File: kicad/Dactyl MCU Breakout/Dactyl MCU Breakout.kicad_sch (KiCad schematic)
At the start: 0 parts

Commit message: feat: schema and board: matrix display led split
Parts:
- added D1, D2, D3, D4: SK6812-MINI-E, Dactyl:SK6812-MINI-E-Dog2, symbol Dactyl:SK6812-MINI-E
- added H1, H2: MountingHole, MountingHole:MountingHole_3.2mm_M3_DIN965_Pad, symbol Mechanical:MountingHole
- added H3: MountingHole, Dactyl:ToolingHole_1.152mm, symbol Mechanical:MountingHole
- added J1: Columns, Connector_PinHeader_2.54mm:PinHeader_1x06_P2.54mm_Vertical, symbol Connector_Generic:Conn_01x06
- added J2: Rows, Connector_PinHeader_2.54mm:PinHeader_1x06_P2.54mm_Vertical, symbol Connector_Generic:Conn_01x06
- added J3: Thumbs, Connector_PinHeader_2.54mm:PinHeader_1x06_P2.54mm_Vertical, symbol Connector_Generic:Conn_01x06
- added J4: Display, Connector_PinHeader_2.54mm:PinHeader_1x05_P2.54mm_Vertical, symbol Connector_Generic:Conn_01x05
- added J5: Split, Connector_PinHeader_2.54mm:PinHeader_1x03_P2.54mm_Vertical, symbol Connector_Generic:Conn_01x03
- added J6: Extrernal, Connector_PinHeader_2.54mm:PinHeader_1x04_P2.54mm_Vertical, symbol Connector_Generic:Conn_01x04
- added J7: JST, Dactyl:JST_PH_S2B-PH-K_1x02_P2.00mm_Horizontal, symbol Dactyl:Conn_01x02_Jump_Two_Side
- added J8: Encoder, Connector_PinHeader_2.54mm:PinHeader_1x02_P2.54mm_Vertical, symbol Connector_Generic:Conn_01x02
- added JP1: LED2 cutoff, Jumper:SolderJumper-2_P1.3mm_Bridged_RoundedPad1.0x1.5mm, symbol Jumper:SolderJumper_2_Bridged
- added JP2: LED3 cutoff, Jumper:SolderJumper-2_P1.3mm_Bridged_RoundedPad1.0x1.5mm, symbol Jumper:SolderJumper_2_Bridged
- added JP3: LED4 cutoff, Jumper:SolderJumper-2_P1.3mm_Bridged_RoundedPad1.0x1.5mm, symbol Jumper:SolderJumper_2_Bridged
- added JP4: External Row Select, Jumper:SolderJumper-3_P1.3mm_Bridged12_RoundedPad1.0x1.5mm, symbol Jumper:SolderJumper_3_Bridged12
- added SW1: Reset, Dactyl:SW_Tactile_SKHL_Angled, symbol Switch:SW_Push
- added SW2: Battery, Dactyl:SW_SPDT_JS202011AQN_wider, symbol Switch:SW_SPDT
- added SW3: LED, Dactyl:SW_SPDT_JS202011AQN_wider, symbol Switch:SW_SPDT
- added U1: ProMicro_r, Dactyl:ProMicro_v2, symbol Dactyl:ProMicro_r
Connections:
- new net: D4.1 (VDD), JP3.2 (B)
- new net: D3.2 (DOUT), D4.4 (DIN)
- new net: J6.4 (Pin_4), JP4.2 (C)
- new net: D2.2 (DOUT), D3.4 (DIN)
- new net: D1.2 (DOUT), D2.4 (DIN)
- new net: D3.1 (VDD), JP2.2 (B), JP3.1 (A)
- new net CS: J4.1 (Pin_1), U1.8 (C6/5)
- new net GND: D1.3 (VSS), D2.3 (VSS), D3.3 (VSS), D4.3 (VSS), J4.2 (Pin_2), J5.3 (Pin_3), J7.GND, SW1.2, U1.23 (GND), U1.3 (GND), U1.4 (GND)
- new net LED: D1.4 (DIN), U1.7 (D4/4)
- new net MOSI: J4.5 (Pin_5), U1.6 (SCL/D0/3)
- new net RAW: J5.2 (Pin_2), SW2.1 (A), U1.24 (RAW)
- new net RST: SW1.1, U1.22 (RST)
- new net SCK: J4.4 (Pin_4), U1.5 (SDA/D1/2)
- new net VCC: J4.3 (Pin_3), SW3.2 (B), U1.21 (VCC)
- new net VCC_LED1: D1.1 (VDD), JP1.1 (A), SW3.1 (A)
- new net VCC_LED2: D2.1 (VDD), JP1.2 (B), JP2.1 (A)
- new net bat+: J7.Pos, SW2.2 (B)
- new net col0: J1.1 (Pin_1), J3.1 (Pin_1), J6.1 (Pin_1), U1.20 (A3/F4)
- new net col1: J1.2 (Pin_2), J3.2 (Pin_2), U1.19 (A2/F5)
- new net col2: J1.3 (Pin_3), J3.3 (Pin_3), U1.18 (A1/F6)
- new net col3: J1.4 (Pin_4), J3.4 (Pin_4), U1.17 (A0/F7)
- new net col4: J1.5 (Pin_5), J3.5 (Pin_5), J6.2 (Pin_2), U1.16 (15/B1)
- new net col5: J1.6 (Pin_6), J6.3 (Pin_3), U1.15 (14/B3)
- new net data: J5.1 (Pin_1), U1.2 (D2/RX1)
- new net enc_b: J8.2 (Pin_2), U1.13 (10/B6)
- new net row0: J2.1 (Pin_1), U1.1 (D3/TX0)
- new net row1: J2.2 (Pin_2), U1.9 (D7/6)
- new net row2: J2.3 (Pin_3), U1.10 (E6/7)
- new net row3: J3.6 (Pin_6), U1.11 (B4/8)
- new net row4: J2.5 (Pin_5), JP4.1 (A), U1.12 (B5/9)
- new net row5: J2.6 (Pin_6), J8.1 (Pin_1), JP4.3 (B), U1.14 (16/B2)
- no-connect marks 0 -> 4
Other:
- note added: "${TITLE}"
- note added: "3.3 v"
- note added: "5 v"
- note added: "Battery"
- note added: "Case back PCB panel left: Reset | center up: USB | right: Battery"
- note added: "Column 6 (or extra)"
- note added: "Columns"
- note added: "ESD: - On split data lines QMK: - handedness solder jumper and diode Extra pins breakout - Encoder pullout for thumb?"
- note added: "Encoder, Row num (or extra)"
- note added: "Expansion"
- note added: "Extra bottom edge MCU pins fiducials for PCBA"
- note added: "Goals - Amoeba matrix, display and breakout separate from case, so case can evolve. - MCU separates from breakout so old keyboards can down grade to wired. - Extenal reset, battery switch and LEDs may stay with old case."
- note added: "Headers"
- note added: "Headers for case mount of: - Reset - Battery switch - Led"
- note added: "Key Matrix"
- note added: "LED"
- note added: "Later"
- note added: "MCU Nice!Nano / ProMicro"
- note added: "Mounts"
- note added: "On board"
- note added: "Reset"
- note added: "Row letter"
- note added: "Rows letters and thumb Row utility (or extra)"
- note added: "SPI SPI LED (or extra) SPI"
- note added: "Split (or extra)"
- note added: "System"
- note added: "User interactions: - USB flash/type/charge on MCU - Reset for flash - Display/LED - Battery on/off - Split cable"
- note added: "Wired"
- title: (none) -> Dactyl MCU Breakout

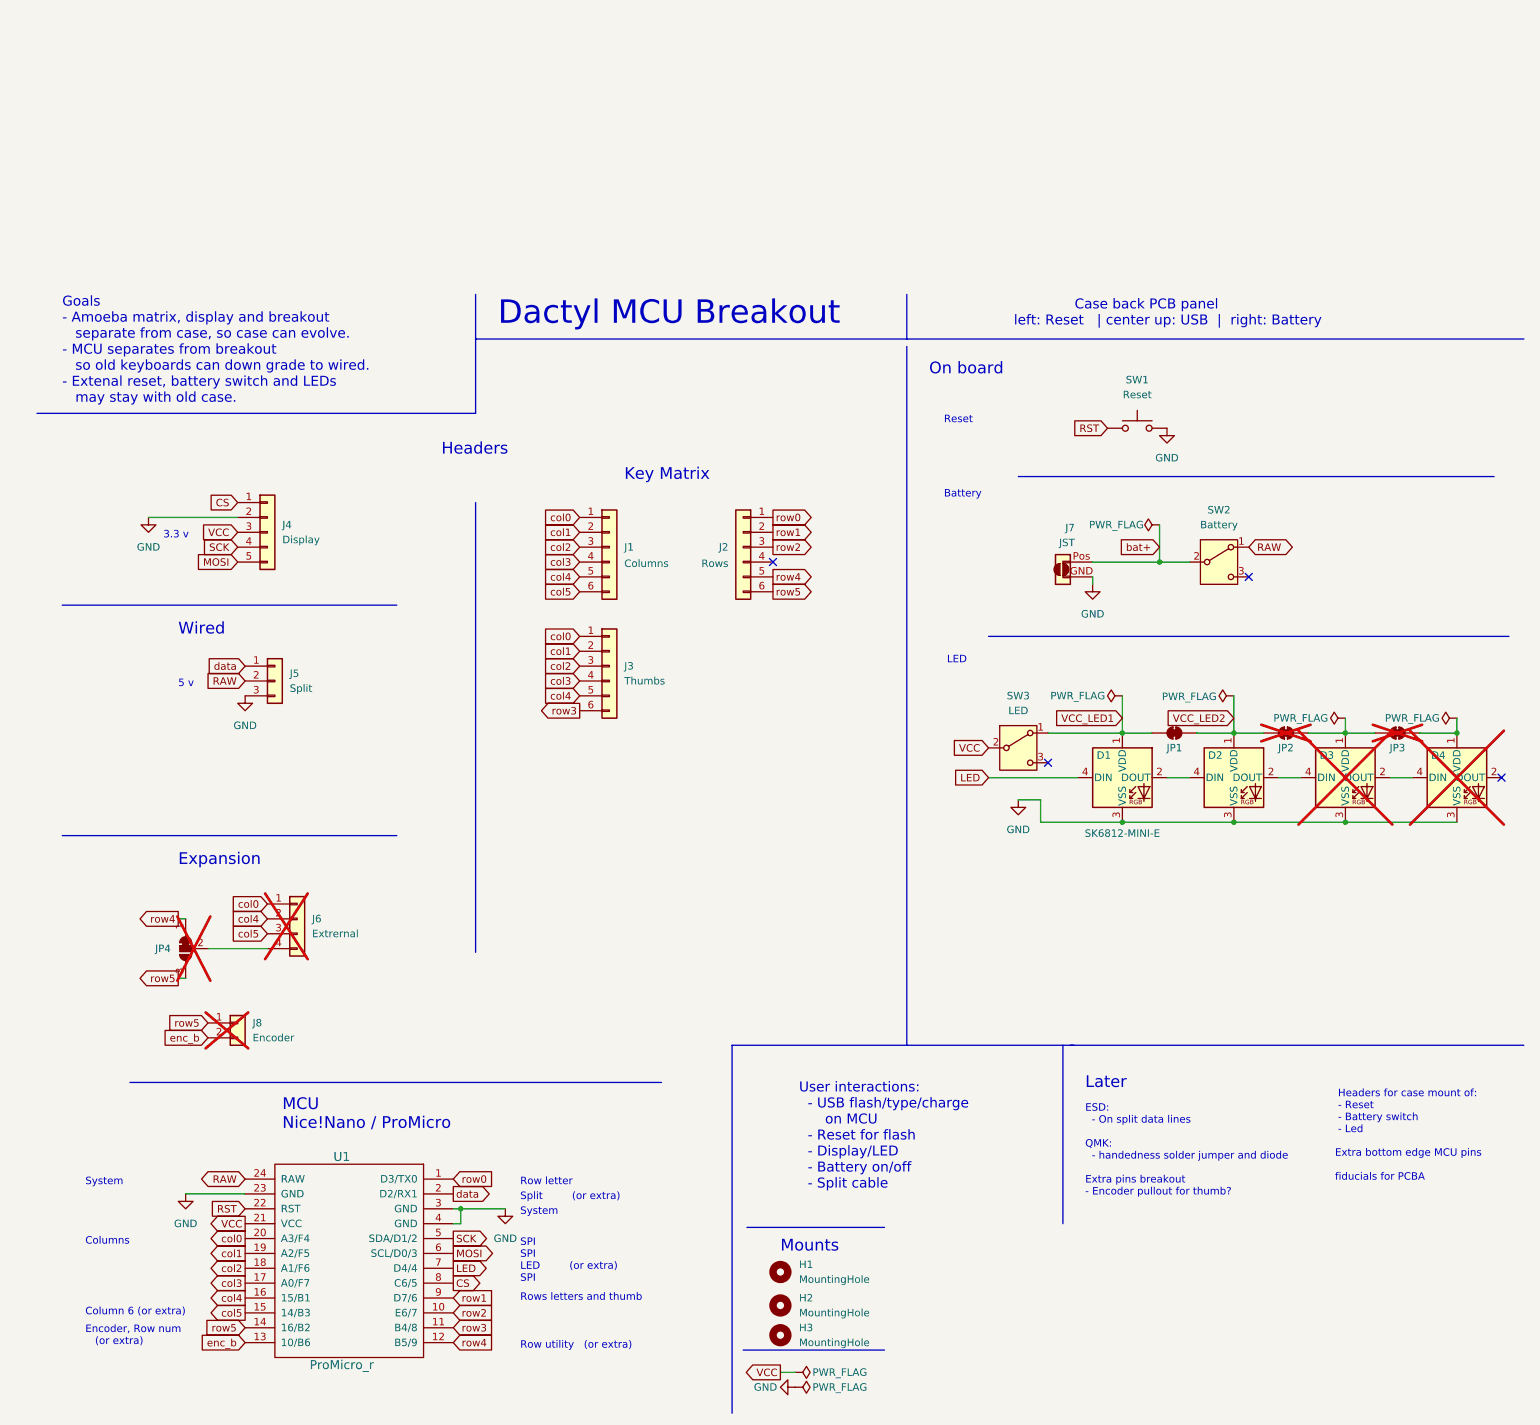
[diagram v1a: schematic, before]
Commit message: feat: jumpered MCU, Vik, shift register, external
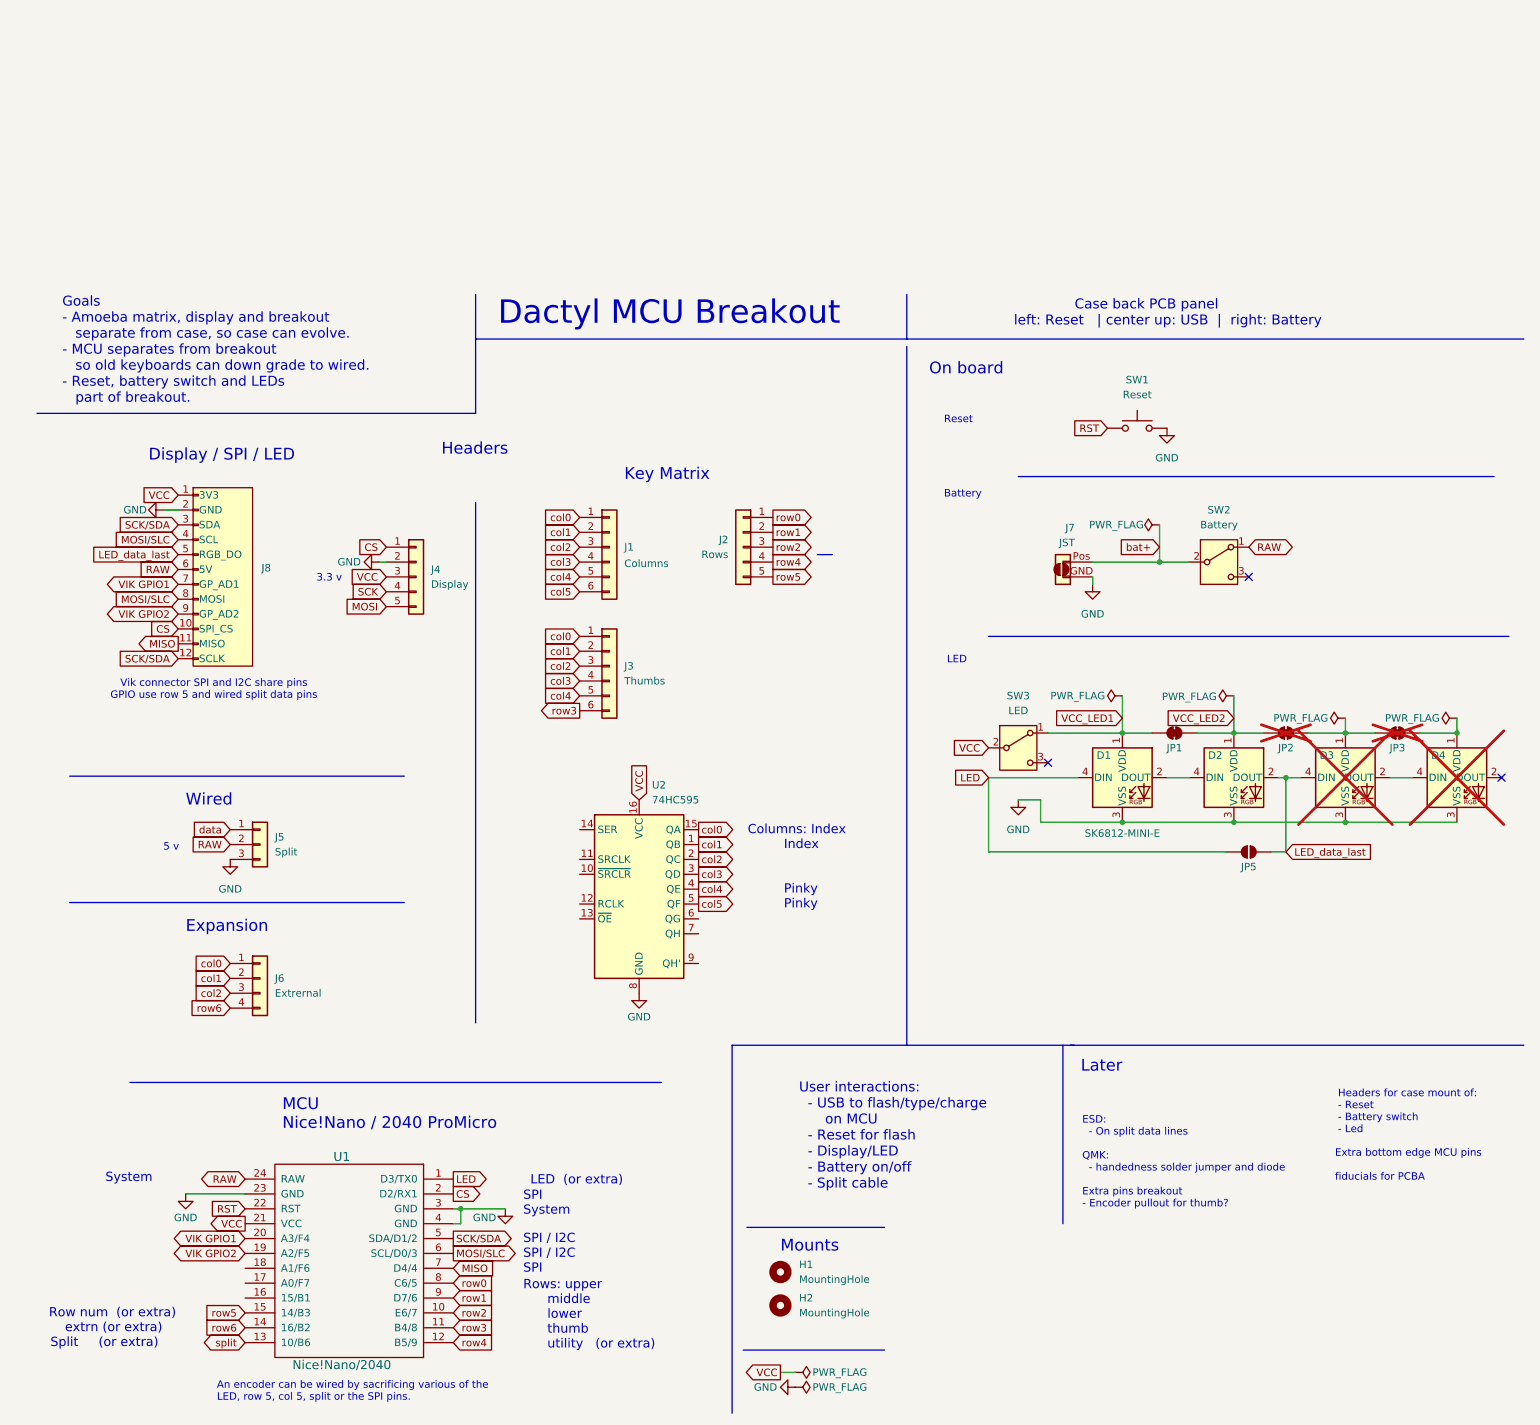
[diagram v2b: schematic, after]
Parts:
- removed H3: MountingHole, Dactyl:ToolingHole_1.152mm, symbol Mechanical:MountingHole
- removed J2: Rows, Connector_PinHeader_2.54mm:PinHeader_1x06_P2.54mm_Vertical, symbol Connector_Generic:Conn_01x06
- removed J8: Encoder, Connector_PinHeader_2.54mm:PinHeader_1x02_P2.54mm_Vertical, symbol Connector_Generic:Conn_01x02
- removed JP4: External Row Select, Jumper:SolderJumper-3_P1.3mm_Bridged12_RoundedPad1.0x1.5mm, symbol Jumper:SolderJumper_3_Bridged12
- added J2: Rows, Connector_PinHeader_2.54mm:PinHeader_1x05_P2.54mm_Vertical, symbol Connector_Generic:Conn_01x05
- added J8: ~, symbol Dactyl:vik-keyboard-connector
- added JP5: LED2 cutoff, Jumper:SolderJumper-2_P1.3mm_Bridged_RoundedPad1.0x1.5mm, symbol Jumper:SolderJumper_2_Open
- added U2: 74HC595, symbol 74xx:74HC595
- J6: now fitted
- U1: value ProMicro_r -> Nice!Nano/2040; footprint Dactyl:ProMicro_v2 -> Dactyl:ProMicro_unrouted
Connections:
- net CS: now also U1.2 (D2/RX1), J8.10 (SPI_CS); no longer U1.8 (C6/5)
- net GND: now also J8.2 (GND), U2.8 (GND)
- net LED: now also U1.1 (D3/TX0), JP5.1 (A); no longer U1.7 (D4/4)
- net MOSI: no longer U1.6 (SCL/D0/3)
- net RAW: now also J8.6 (5V)
- net SCK: no longer U1.5 (SDA/D1/2)
- net VCC: now also J8.1 (3V3), U2.16 (VCC)
- net col0: now also U2.15 (QA); no longer U1.20 (A3/F4)
- net col1: now also J6.2 (Pin_2), U2.1 (QB); no longer U1.19 (A2/F5)
- net col2: now also J6.3 (Pin_3), U2.2 (QC); no longer U1.18 (A1/F6)
- net col3: now also U2.3 (QD); no longer U1.17 (A0/F7)
- net col4: now also U2.4 (QE); no longer J6.2 (Pin_2), U1.16 (15/B1)
- net col5: now also U2.5 (QF); no longer J6.3 (Pin_3), U1.15 (14/B3)
- net data: no longer U1.2 (D2/RX1)
- net row0: now also U1.8 (C6/5), J2.1 (Pin_1); no longer U1.1 (D3/TX0)
- net row1: now also J2.2 (Pin_2)
- net row2: now also J2.3 (Pin_3)
- net row4: now also J2.4 (Pin_4)
- net row5: now also U1.15 (14/B3), J2.5 (Pin_5); no longer U1.14 (16/B2)
- net row6: now reaches J6.4 (Pin_4)
- net row6: now also U1.14 (16/B2)
- net LED_data_last: now reaches D2.2 (DOUT), D3.4 (DIN)
- net LED_data_last: now also J8.5 (RGB_DO), JP5.2 (B)
- net enc_b renamed split
- new net MISO: J8.11 (MISO), U1.7 (D4/4)
- new net MOSI/SLC: J8.4 (SCL), J8.8 (MOSI), U1.6 (SCL/D0/3)
- new net SCK/SDA: J8.12 (SCLK), J8.3 (SDA), U1.5 (SDA/D1/2)
- new net VIK GPIO1: J8.7 (GP_AD1), U1.20 (A3/F4)
- new net VIK GPIO2: J8.9 (GP_AD2), U1.19 (A2/F5)
- no-connect marks 4 -> 3
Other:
- note added: "An encoder can be wired by sacrificing various of the LED, row 5, col 5, split or the SPI pins."
- note added: "Columns: Index Index Pinky Pinky"
- note added: "Display / SPI / LED"
- note added: "Goals - Amoeba matrix, display and breakout separate from case, so case can evolve. - MCU separates from breakout so old keyboards can down grade to wired. - Reset, battery switch and LEDs part of breakout."
- note added: "LED (or extra)"
- note added: "MCU Nice!Nano / 2040 ProMicro"
- note added: "Row num (or extra) extrn (or extra)"
- note added: "Rows: upper middle lower thumb utility (or extra)"
- note added: "SPI"
- note added: "SPI / I2C SPI / I2C SPI"
- note added: "User interactions: - USB to flash/type/charge on MCU - Reset for flash - Display/LED - Battery on/off - Split cable"
- note added: "Vik connector SPI and I2C share pins GPIO use row 5 and wired split data pins"
- note removed: "Column 6 (or extra)"
- note removed: "Columns"
- note removed: "Encoder, Row num (or extra)"
- note removed: "Goals - Amoeba matrix, display and breakout separate from case, so case can evolve. - MCU separates from breakout so old keyboards can down grade to wired. - Extenal reset, battery switch and LEDs may stay with old case."
- note removed: "MCU Nice!Nano / ProMicro"
- note removed: "Row letter"
- note removed: "Rows letters and thumb Row utility (or extra)"
- note removed: "SPI SPI LED (or extra) SPI"
- note removed: "User interactions: - USB flash/type/charge on MCU - Reset for flash - Display/LED - Battery on/off - Split cable"
- moved on the sheet: J4, J5
